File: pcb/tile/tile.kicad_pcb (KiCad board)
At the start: 2 copper layers, 21.4 x 30.7 mm, 15 parts, among them IC1 THVD1420DR, J1 LED Strip, J2 UPDI, J5 12V, J6 RS-485 Jack, U1 ATtiny3224-X

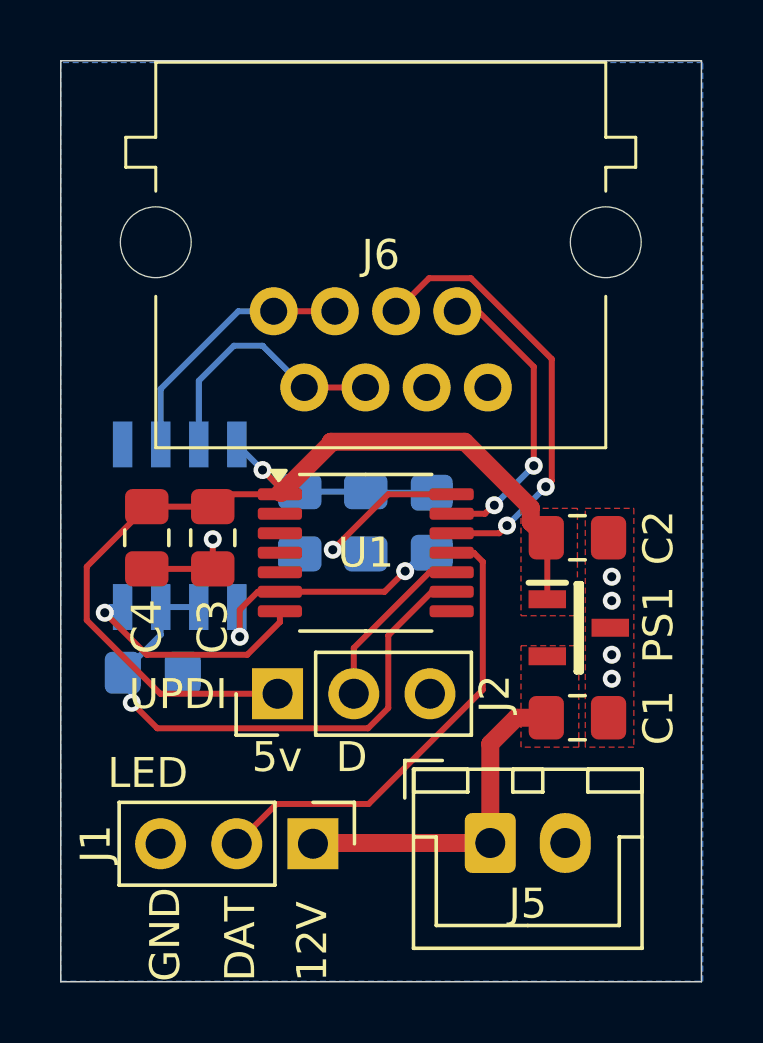
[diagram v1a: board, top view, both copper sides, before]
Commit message: Slightly widened the 12V trace between the power in and strip
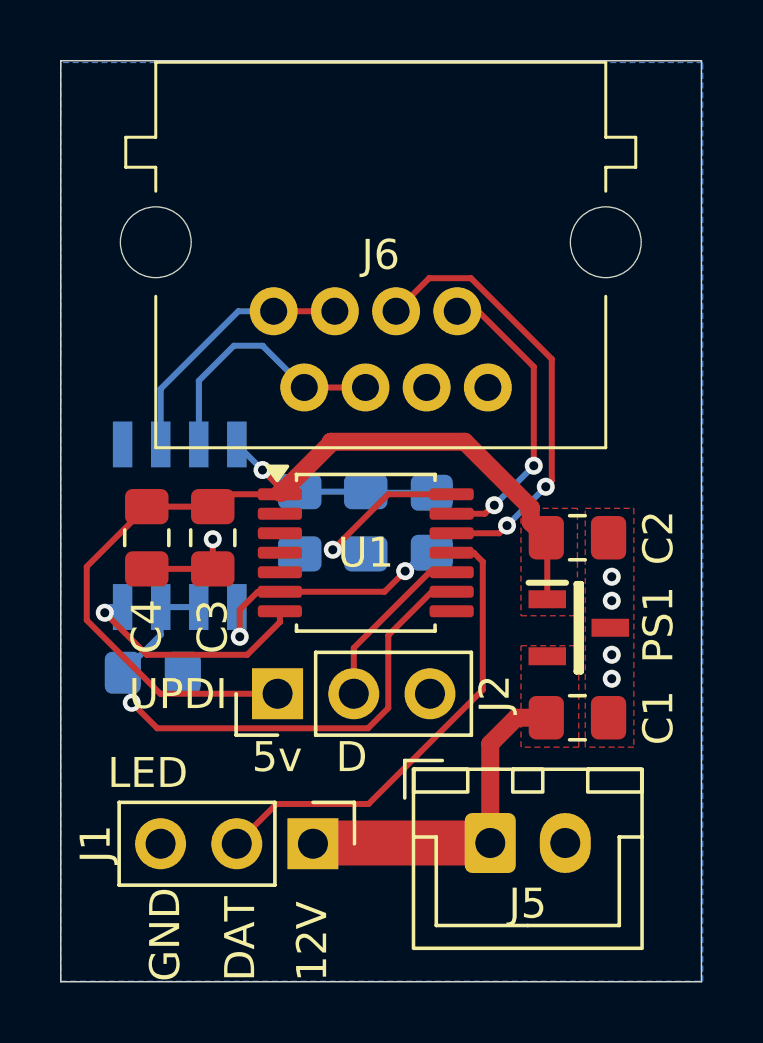
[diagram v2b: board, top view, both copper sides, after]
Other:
- board text added: "v1.2 2026-06-18"
- board text removed: "v1.1a 2025-10-18"
